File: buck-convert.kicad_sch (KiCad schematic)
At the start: 1 part, among them U5 LMR16006YQ

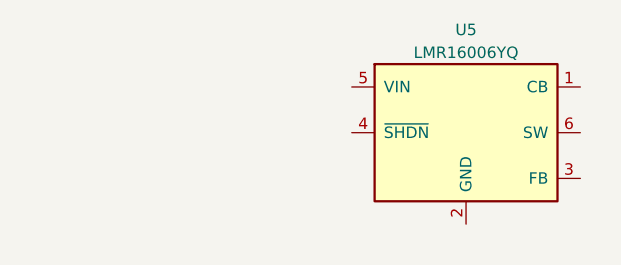
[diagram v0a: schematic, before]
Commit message: Remove dup folder
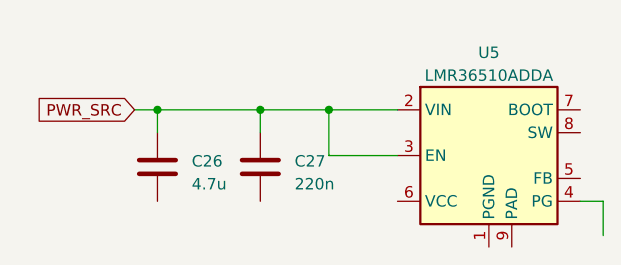
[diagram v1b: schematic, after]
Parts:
- removed U5: LMR16006YQ, Package_TO_SOT_SMD:SOT-23-6, symbol Regulator_Switching:LMR16006YQ
- added C26: 4.7u, symbol Device:C
- added C27: 220n, symbol Device:C
- added U5: LMR36510ADDA, Package_SO:Texas_HTSOP-8-1EP_3.9x4.9mm_P1.27mm_EP2.95x4.9mm_Mask2.4x3.1mm_ThermalVias, symbol Regulator_Switching:LMR36510ADDA
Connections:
- new net PWR_SRC: C26.1, C27.1, U5.2 (VIN), U5.3 (EN)
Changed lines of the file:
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@@
 (kicad_sch (version 20230121) (generator eeschema)
   (paper "A4")
-  (symbol (lib_id "Regulator_Switching:LMR16006YQ") (at 142.24 77.47 0) (unit 1)
+  (junction (at 119.38 74.93) (diameter 0) (color 0 0 0 0)
+  )
+  (junction (at 107.95 74.93) (diameter 0) (color 0 0 0 0)
+  )
+  (junction (at 127 74.93) (diameter 0) (color 0 0 0 0)
+  )
+  (wire (pts (xy 107.95 74.93) (xy 107.95 77.47))
+    (stroke (width 0) (type default))
+  )
+  (wire (pts (xy 107.95 74.93) (xy 119.38 74.93))
+    (stroke (width 0) (type default))
+  )
+  (wire (pts (xy 157.48 85.09) (xy 157.48 88.9))
+    (stroke (width 0) (type default))
+  )
+  (wire (pts (xy 127 74.93) (xy 134.62 74.93))
+    (stroke (width 0) (type default))
+  )
+  (wire (pts (xy 119.38 74.93) (xy 127 74.93))
+    (stroke (width 0) (type default))
+  )
+  (wire (pts (xy 105.41 74.93) (xy 107.95 74.93))
+    (stroke (width 0) (type default))
+  )
+  (wire (pts (xy 119.38 74.93) (xy 119.38 77.47))
+    (stroke (width 0) (type default))
+  )
+  (wire (pts (xy 127 80.01) (xy 127 74.93))
+    (stroke (width 0) (type default))
+  )
+  (wire (pts (xy 134.62 80.01) (xy 127 80.01))
+    (stroke (width 0) (type default))
+  )
+  (wire (pts (xy 154.94 85.09) (xy 157.48 85.09))
+    (stroke (width 0) (type default))
+  )
+  (global_label "PWR_SRC" (shape input) (at 105.41 74.93 180) (fields_autoplaced)
+    (effects (font (size 1.27 1.27)) (justify right))
+    (property "Intersheetrefs" "${INTERSHEET_REFS}" (at 93.7957 74.93 0)
+      (effects (font (size 1.27 1.27)) (justify right) hide)
+    )
+  )
+  (symbol (lib_id "Device:C") (at 119.38 81.28 0) (unit 1)
     (in_bom yes) (on_board yes) (dnp no) (fields_autoplaced)
-    (property "Reference" "U5" (at 142.24 66.04 0)
+    (property "Reference" "C27" (at 123.19 80.645 0)
+      (effects (font (size 1.27 1.27)) (justify left))
+    )
+    (property "Value" "220n" (at 123.19 83.185 0)
+      (effects (font (size 1.27 1.27)) (justify left))
+    )
+    (property "Footprint" "" (at 120.3452 85.09 0)
+      (effects (font (size 1.27 1.27)) hide)
+    )
+    (property "Datasheet" "~" (at 119.38 81.28 0)
+      (effects (font (size 1.27 1.27)) hide)
+    )
+    (pin "1")
+    (pin "2")
+    (instances
+      (project "electrium-esc-v2"
+        (path "/be00c12c-11fa-42cb-8a0b-46fcd24b2ced/dedba472-5e9c-489a-b80e-963af35f7eb6"
+          (reference "C27") (unit 1)
+        )
+      )
+    )
+  )
+  (symbol (lib_id "Regulator_Switching:LMR36510ADDA") (at 144.78 80.01 0) (unit 1)
+    (in_bom yes) (on_board yes) (dnp no) (fields_autoplaced)
+    (property "Reference" "U5" (at 144.78 68.58 0)
       (effects (font (size 1.27 1.27)))
     )
-    (property "Value" "LMR16006YQ" (at 142.24 68.58 0)
+    (property "Value" "LMR36510ADDA" (at 144.78 71.12 0)
       (effects (font (size 1.27 1.27)))
     )
-    (property "Footprint" "Package_TO_SOT_SMD:SOT-23-6" (at 142.24 90.17 0)
-      (effects (font (size 1.27 1.27) italic) hide)
+    (property "Footprint" "Package_SO:Texas_HTSOP-8-1EP_3.9x4.9mm_P1.27mm_EP2.95x4.9mm_Mask2.4x3.1mm_ThermalVias" (at 144.78 100.33 0)
+      (effects (font (size 1.27 1.27)) hide)
     )
-    (property "Datasheet" "http://www.ti.com/lit/ds/symlink/lmr16006y-q1.pdf" (at 132.08 66.04 0)
+    (property "Datasheet" "http://www.ti.com/lit/ds/symlink/lmr36510.pdf" (at 144.78 81.28 0)
       (effects (font (size 1.27 1.27)) hide)
     )
@@
     (pin "5")
     (pin "6")
+    (pin "7")
+    (pin "8")
+    (pin "9")
     (instances
       (project "electrium-esc-v2"
@@
         )
       )
+    )
+  )
+  (symbol (lib_id "Device:C") (at 107.95 81.28 0) (unit 1)
+    (in_bom yes) (on_board yes) (dnp no) (fields_autoplaced)
+    (property "Reference" "C26" (at 111.76 80.645 0)
+      (effects (font (size 1.27 1.27)) (justify left))
+    )
+    (property "Value" "4.7u" (at 111.76 83.185 0)
+      (effects (font (size 1.27 1.27)) (justify left))
+    )
+    (property "Footprint" "" (at 108.9152 85.09 0)
+      (effects (font (size 1.27 1.27)) hide)
+    )
+    (property "Datasheet" "~" (at 107.95 81.28 0)
+      (effects (font (size 1.27 1.27)) hide)
+    )
+    (pin "1")
+    (pin "2")
+    (instances
+      (project "electrium-esc-v2"
+        (path "/be00c12c-11fa-42cb-8a0b-46fcd24b2ced/dedba472-5e9c-489a-b80e-963af35f7eb6"
+          (reference "C26") (unit 1)
+        )
+      )

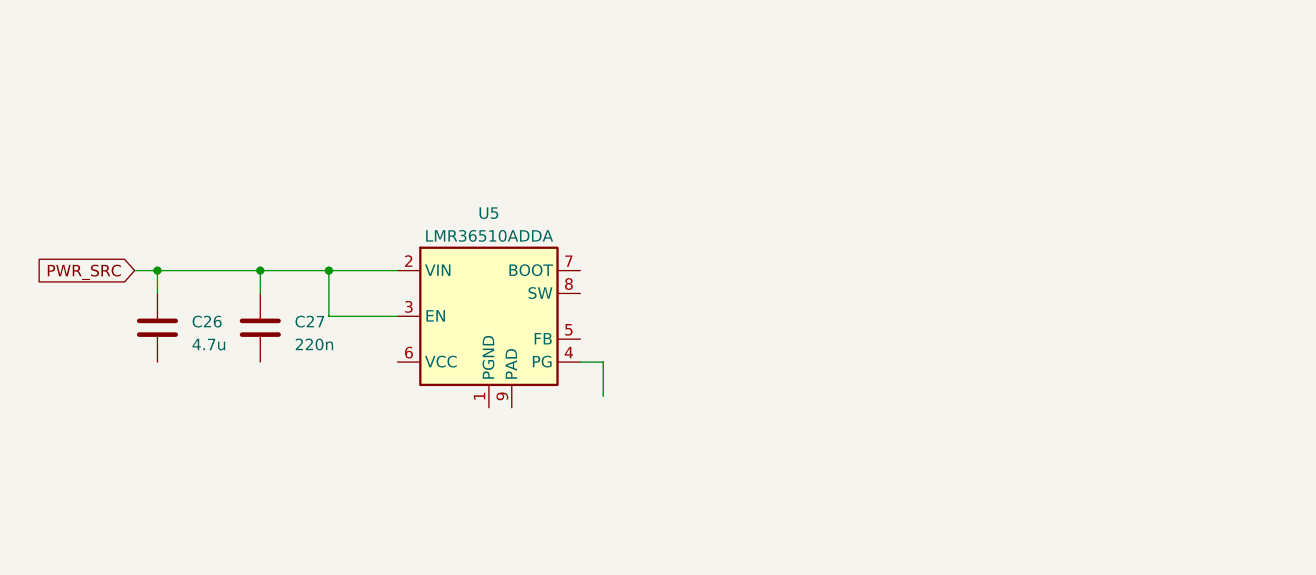
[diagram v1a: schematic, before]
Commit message: Add buck converter schematic
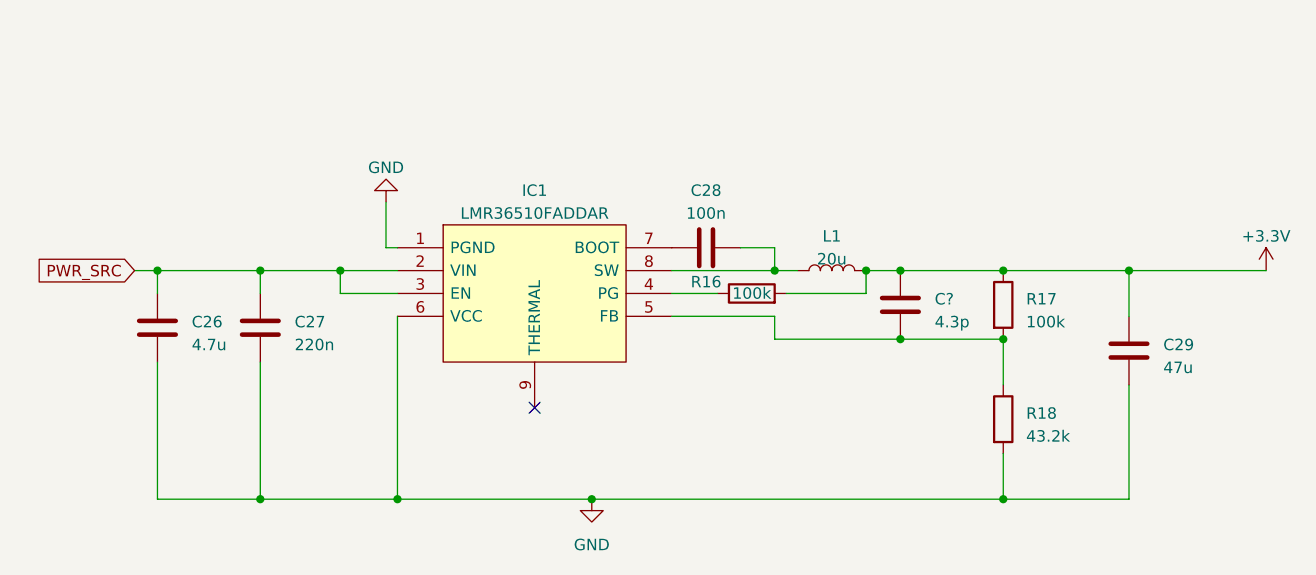
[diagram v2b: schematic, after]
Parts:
- removed U5: LMR36510ADDA, Package_SO:Texas_HTSOP-8-1EP_3.9x4.9mm_P1.27mm_EP2.95x4.9mm_Mask2.4x3.1mm_ThermalVias, symbol Regulator_Switching:LMR36510ADDA
- added C28: 100n, symbol Device:C
- added C29: 47u, symbol Device:C
- added C?: 4.3p, symbol Device:C
- added IC1: LMR36510FADDAR, SOIC127P600X170-9N, symbol LMR36510FADDAR:LMR36510FADDAR
- added L1: 20u, symbol Device:L
- added R16, R17: 100k, symbol Device:R
- added R18: 43.2k, symbol Device:R
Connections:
- net PWR_SRC: now also IC1.2 (VIN), IC1.3 (EN)
- net GND: now reaches C27.2
- net GND: now also C26.2, C29.1, IC1.1 (PGND), IC1.6 (VCC), R18.2
- new net: IC1.4 (PG), R16.1
- new net: C?.1, IC1.5 (FB), R17.2, R18.1
- new net: C28.1, IC1.7 (BOOT)
- new net: C28.2, IC1.8 (SW), L1.1
- new net +3.3V: C29.2, C?.2, L1.2, R16.2, R17.1
- no-connect marks 0 -> 1

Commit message: Fix a few errors
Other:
- moved on the sheet: C28
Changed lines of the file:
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@@
   (junction (at 156.21 100.33) (diameter 0) (color 0 0 0 0)
+  )
+  (junction (at 224.79 74.93) (diameter 0) (color 0 0 0 0)
   )
   (junction (at 201.93 74.93) (diameter 0) (color 0 0 0 0)
@@
     (stroke (width 0) (type default))
   )
+  (wire (pts (xy 167.64 72.39) (xy 165.1 72.39))
+    (stroke (width 0) (type default))
+  )
   (wire (pts (xy 176.53 74.93) (xy 179.07 74.93))
     (stroke (width 0) (type default))
   )
+  (wire (pts (xy 224.79 74.93) (xy 231.14 74.93))
+    (stroke (width 0) (type default))
+  )
   (wire (pts (xy 186.69 74.93) (xy 190.5 74.93))
     (stroke (width 0) (type default))
@@
     (stroke (width 0) (type default))
   )
-  (wire (pts (xy 215.9 74.93) (xy 231.14 74.93))
-    (stroke (width 0) (type default))
-  )
-  (wire (pts (xy 172.72 72.39) (xy 176.53 72.39))
+  (wire (pts (xy 215.9 74.93) (xy 224.79 74.93))
+    (stroke (width 0) (type default))
+  )
+  (wire (pts (xy 175.26 72.39) (xy 176.53 72.39))
     (stroke (width 0) (type default))
   )
@@
         (path "/be00c12c-11fa-42cb-8a0b-46fcd24b2ced/dedba472-5e9c-489a-b80e-963af35f7eb6"
           (reference "C29") (unit 1)
+        )
+      )
+    )
+  )
+  (symbol (lib_id "power:PWR_FLAG") (at 224.79 74.93 0) (unit 1)
+    (in_bom yes) (on_board yes) (dnp no) (fields_autoplaced)
+    (property "Reference" "#FLG02" (at 224.79 73.025 0)
+      (effects (font (size 1.27 1.27)) hide)
+    )
+    (property "Value" "PWR_FLAG" (at 224.79 71.12 0)
+      (effects (font (size 1.27 1.27)) hide)
+    )
+    (property "Footprint" "" (at 224.79 74.93 0)
+      (effects (font (size 1.27 1.27)) hide)
+    )
+    (property "Datasheet" "~" (at 224.79 74.93 0)
+      (effects (font (size 1.27 1.27)) hide)
+    )
+    (pin "1")
+    (instances
+      (project "electrium-esc-v2"
+        (path "/be00c12c-11fa-42cb-8a0b-46fcd24b2ced/dedba472-5e9c-489a-b80e-963af35f7eb6"
+          (reference "#FLG02") (unit 1)
         )
       )
@@
     )
   )
-  (symbol (lib_id "Device:C") (at 168.91 72.39 90) (unit 1)
-    (in_bom yes) (on_board yes) (dnp no) (fields_autoplaced)
-    (property "Reference" "C28" (at 168.91 66.04 90)
-      (effects (font (size 1.27 1.27)))
-    )
-    (property "Value" "100n" (at 168.91 68.58 90)
-      (effects (font (size 1.27 1.27)))
-    )
-    (property "Footprint" "" (at 172.72 71.4248 0)
-      (effects (font (size 1.27 1.27)) hide)
-    )
-    (property "Datasheet" "~" (at 168.91 72.39 0)
-      (effects (font (size 1.27 1.27)) hide)
-    )
+  (symbol (lib_id "Device:C") (at 171.45 72.39 90) (unit 1)
+    (in_bom yes) (on_board yes) (dnp no) (fields_autoplaced)
+    (property "Reference" "C28" (at 171.45 66.04 90)
+      (effects (font (size 1.27 1.27)))
+    )
+    (property "Value" "100n" (at 171.45 68.58 90)
+      (effects (font (size 1.27 1.27)))
+    )
+    (property "Footprint" "" (at 175.26 71.4248 0)
+      (effects (font (size 1.27 1.27)) hide)
+    )
+    (property "Datasheet" "~" (at 171.45 72.39 0)
+      (effects (font (size 1.27 1.27)) hide)
+    )
